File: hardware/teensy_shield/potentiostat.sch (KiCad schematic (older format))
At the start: 94 parts, among them K1 CONN_3, P1 CONN_2, P10 CONN_2, P11 CONN_2, P12 CONN_2, P13 CONN_5X2, P14 CONN_5X2, P15 CONN_2X2, P16 CONN_2X2, P17 CONN_2, P18 CONN_2, P19 CONN_2, P2 CONN_2, P20 CONN_2, P21 CONN_2, P3 CONN_2, P4 CONN_2, P5 CONN_2, P6 CONN_2, P7 CONN_2, P8 CONN_2, P9 CONN_2, U1 ZXRE060, U10 OPA227, U11 OP07, U12 LT1995, U13 ADG44X, U2 TEENSY3.1, U3 MAX6176AASA+, U4 LT1995, U5 AD8250, U6 MEA1D05XXSC, U7 OPA129, U8 OPA129, U9 ADG44X

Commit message: Worked on BOM.
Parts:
- C7: value 4.7uf -> 4.7uF
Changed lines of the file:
@@
 Sheet 1 1
 Title ""
-Date "17 nov 2016"
+Date "30 nov 2016"
 Rev ""
 Comp ""
@@
 P 1775 5800
 F 0 "C7" H 1825 5900 50  0000 L CNN
-F 1 "4.7uf" H 1825 5700 50  0000 L CNN
+F 1 "4.7uF" H 1825 5700 50  0000 L CNN
 F 2 "~" H 1775 5800 60  0000 C CNN
 F 3 "~" H 1775 5800 60  0000 C CNN

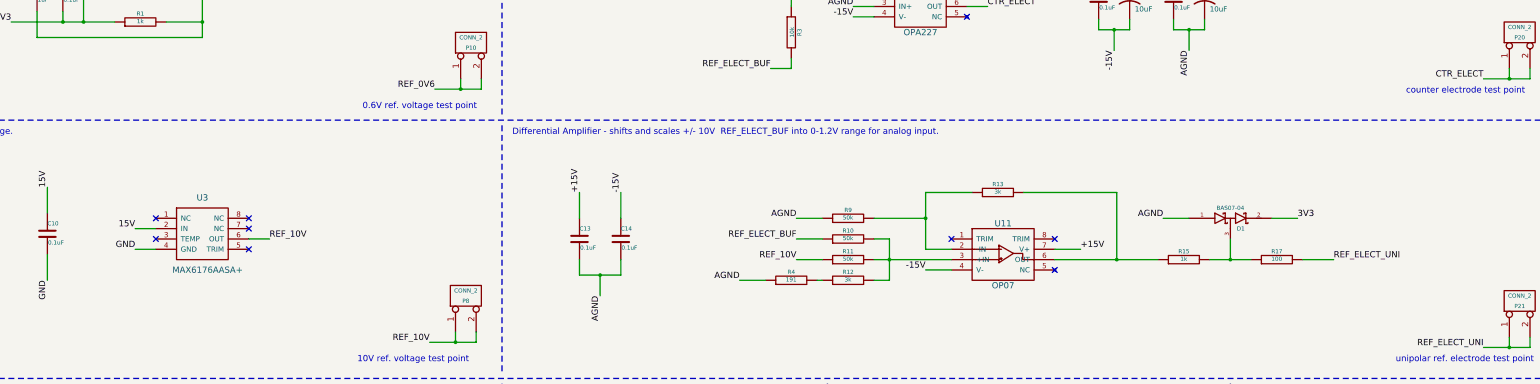
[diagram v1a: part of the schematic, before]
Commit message: Added hgignore file. Added initiall aout test firmware.
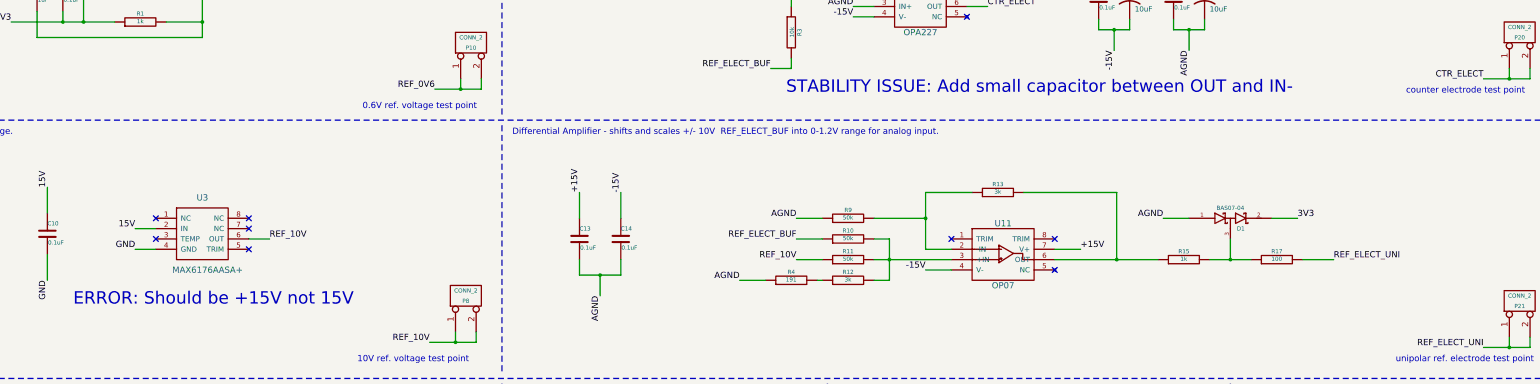
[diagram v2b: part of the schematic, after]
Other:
- note added: "ERROR: Should be +15V not 15V"
- note added: "STABILITY ISSUE: Add small capacitor between OUT and IN-"
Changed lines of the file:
@@
 Sheet 1 1
 Title ""
-Date "30 nov 2016"
+Date "13 dec 2016"
 Rev ""
 Comp ""
@@
 Entry Wire Line
 	2900 8300 3000 8400
+Text Notes 2150 13300 0    120  ~ 0
+ERROR: Should be +15V not 15V
+Text Notes 9050 11250 0    120  ~ 0
+STABILITY ISSUE: Add small capacitor between OUT and IN-
 $EndSCHEMATC

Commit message: Fixed issues schematic. Added new parts to layout. Updated BOM. Board not yet re-routed.
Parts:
- added C39: 10nF, ~, symbol C
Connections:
- net 15V is gone; now on net +15V: C10.1, U3.2 (IN)
- net CTR_ELECT: now also C39.2
- net at R2.2, R3.1, U10.2 (IN-): now also C39.1
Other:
- note removed: "ERROR: Should be +15V not 15V"
- note removed: "STABILITY ISSUE: Add small capacitor between OUT and IN-"
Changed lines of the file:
@@
 Sheet 1 1
 Title ""
-Date "13 dec 2016"
+Date "22 dec 2016"
 Rev ""
 Comp ""
@@
 Text Label 11000 10300 0    60   ~ 0
 +15V
-Wire Wire Line
-	10800 10400 11000 10400
 Text Label 11000 10400 0    60   ~ 0
 CTR_ELECT
@@
 10V Reference voltage.
 Text Label 2750 12550 2    60   ~ 0
-15V
++15V
 Text Label 2750 12750 2    60   ~ 0
 GND
@@
 GND
 Text Label 1900 12150 1    60   ~ 0
-15V
++15V
 $Comp
 L CONN_2 P1
@@
 GND
 $Comp
-L PWR_FLAG #FLG01
+L PWR_FLAG #FLG1
 U 1 1 57EDFCAC
 P 5550 950
-F 0 "#FLG01" H 5550 1045 30  0001 C CNN
+F 0 "#FLG1" H 5550 1045 30  0001 C CNN
 F 1 "PWR_FLAG" H 5550 1130 30  0000 C CNN
 F 2 "" H 5550 950 60  0000 C CNN
@@
 	5550 950  5550 1100
 $Comp
-L PWR_FLAG #FLG02
+L PWR_FLAG #FLG2
 U 1 1 57EE00C1
 P 5550 1650
-F 0 "#FLG02" H 5550 1745 30  0001 C CNN
+F 0 "#FLG2" H 5550 1745 30  0001 C CNN
 F 1 "PWR_FLAG" H 5550 1830 30  0000 C CNN
 F 2 "" H 5550 1650 60  0000 C CNN
@@
 $EndComp
 $Comp
-L PWR_FLAG #FLG03
+L PWR_FLAG #FLG3
 U 1 1 57EE00C7
 P 6000 1650
-F 0 "#FLG03" H 6000 1745 30  0001 C CNN
+F 0 "#FLG3" H 6000 1745 30  0001 C CNN
 F 1 "PWR_FLAG" H 6000 1830 30  0000 C CNN
 F 2 "" H 6000 1650 60  0000 C CNN
@@
 Entry Wire Line
 	2900 8300 3000 8400
-Text Notes 2150 13300 0    120  ~ 0
-ERROR: Should be +15V not 15V
-Text Notes 9050 11250 0    120  ~ 0
-STABILITY ISSUE: Add small capacitor between OUT and IN-
+$Comp
+L C C39
+U 1 1 585C345D
+P 10350 9700
+F 0 "C39" H 10350 9800 40  0000 L CNN
+F 1 "10nF" H 10356 9615 40  0000 L CNN
+F 2 "~" H 10388 9550 30  0000 C CNN
+F 3 "~" H 10350 9700 60  0000 C CNN
+	1    10350 9700
+	0    -1   -1   0
+$EndComp
+Wire Wire Line
+	10800 10400 11000 10400
+Wire Wire Line
+	9800 9700 10150 9700
+Wire Wire Line
+	10550 9700 10900 9700
+Wire Wire Line
+	10900 9700 10900 10400
+Connection ~ 10900 10400
+Wire Wire Line
+	9800 9700 9800 10300
+Connection ~ 9800 10300
 $EndSCHEMATC

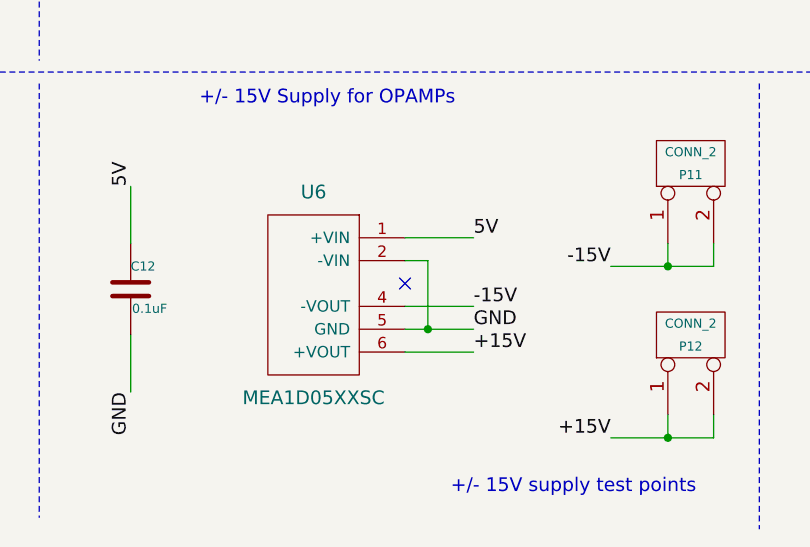
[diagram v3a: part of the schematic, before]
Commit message: Modified teensy shield BOM, layout, and gerbers per pcb manufacturers suggestions.
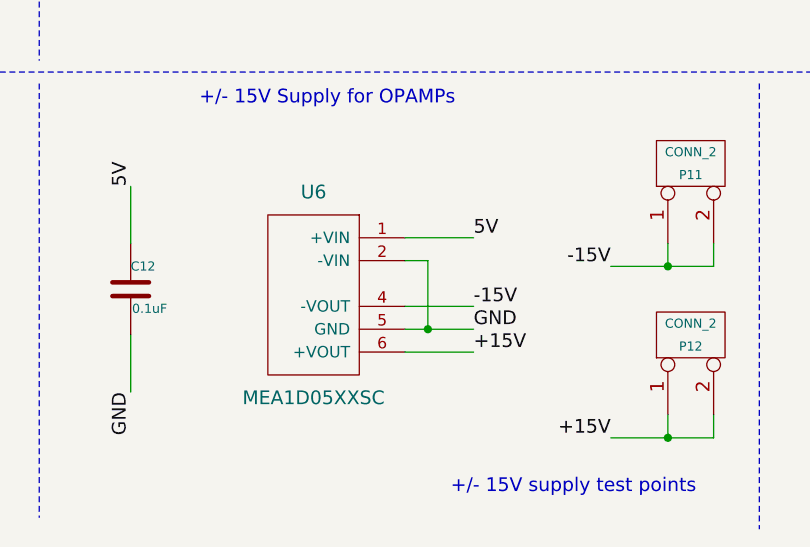
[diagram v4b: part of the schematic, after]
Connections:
- no-connect marks 35 -> 34
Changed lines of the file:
@@
 Sheet 1 1
 Title ""
-Date "22 dec 2016"
+Date "3 jan 2017"
 Rev ""
 Comp ""
@@
 Text Label 8200 15125 0    60   ~ 0
 GND
-NoConn ~ 7900 14925
 Text Label 8200 15025 0    60   ~ 0
 -15V
@@
 GND
 $Comp
-L PWR_FLAG #FLG1
+L PWR_FLAG #FLG01
 U 1 1 57EDFCAC
 P 5550 950
-F 0 "#FLG1" H 5550 1045 30  0001 C CNN
+F 0 "#FLG01" H 5550 1045 30  0001 C CNN
 F 1 "PWR_FLAG" H 5550 1130 30  0000 C CNN
 F 2 "" H 5550 950 60  0000 C CNN
@@
 	5550 950  5550 1100
 $Comp
-L PWR_FLAG #FLG2
+L PWR_FLAG #FLG02
 U 1 1 57EE00C1
 P 5550 1650
-F 0 "#FLG2" H 5550 1745 30  0001 C CNN
+F 0 "#FLG02" H 5550 1745 30  0001 C CNN
 F 1 "PWR_FLAG" H 5550 1830 30  0000 C CNN
 F 2 "" H 5550 1650 60  0000 C CNN
@@
 $EndComp
 $Comp
-L PWR_FLAG #FLG3
+L PWR_FLAG #FLG03
 U 1 1 57EE00C7
 P 6000 1650
-F 0 "#FLG3" H 6000 1745 30  0001 C CNN
+F 0 "#FLG03" H 6000 1745 30  0001 C CNN
 F 1 "PWR_FLAG" H 6000 1830 30  0000 C CNN
 F 2 "" H 6000 1650 60  0000 C CNN
